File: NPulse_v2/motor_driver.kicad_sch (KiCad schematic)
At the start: 16 parts, among them J1 Screw_Terminal_01x02, Q1 PMOS, Q2 PMOS, Q3 NMOS, Q4 NMOS

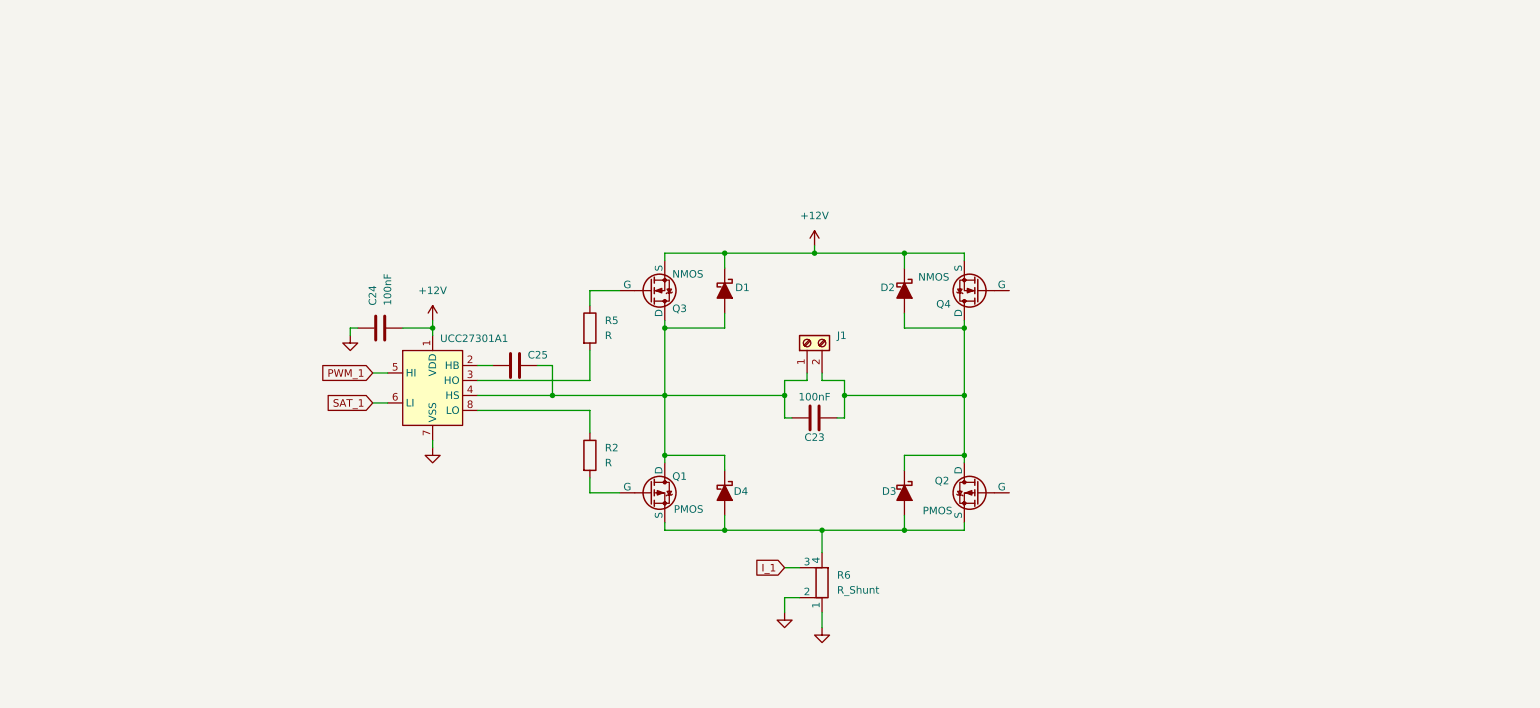
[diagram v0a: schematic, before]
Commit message: Add MCU, FSR, motor drivers, light sensing
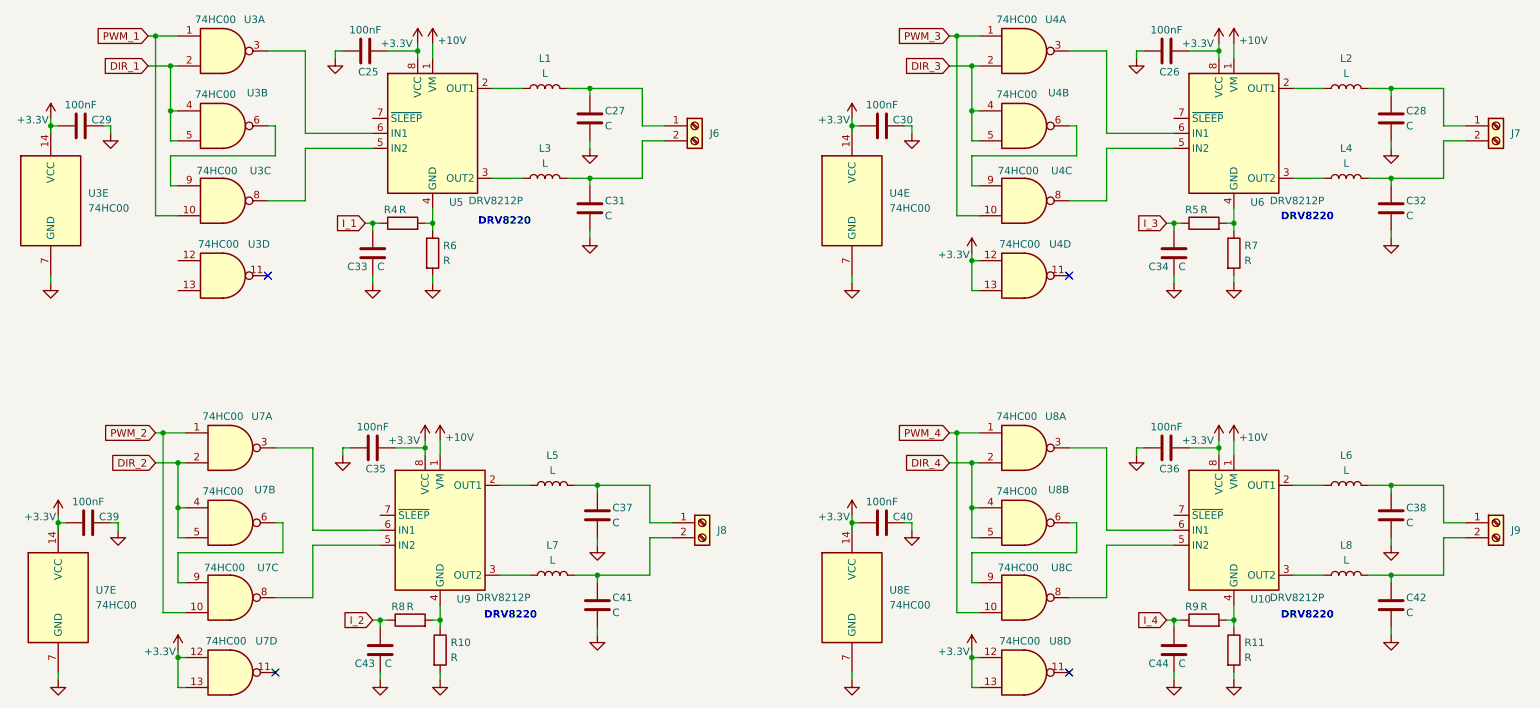
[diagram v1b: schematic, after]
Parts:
- removed C23, C24: 100nF, symbol Device:C
- removed D1, D2, D3, D4: D_Schottky_Filled, symbol Device:D_Schottky_Filled
- removed J1: Screw_Terminal_01x02, symbol Connector:Screw_Terminal_01x02
- removed Q1, Q2: PMOS, symbol Simulation_SPICE:PMOS
- removed Q3, Q4: NMOS, symbol Simulation_SPICE:NMOS
- removed R2: R, symbol Device:R
- removed R6: R_Shunt, symbol Device:R_Shunt
- removed UCC27301A1: U, symbol Driver_FET:UCC27301A
- added C26, C29, C30, C35, C36, C39, C40: 100nF, symbol Device:C
- added C27, C28, C31, C32, C33, C34, C37, C38, C41, C42, C43, C44: C, symbol Device:C
- added J6, J7, J8, J9: Screw_Terminal_01x02, symbol Connector:Screw_Terminal_01x02
- added L1, L2, L3, L4, L5, L6, L7, L8: L, symbol Device:L
- added R10, R11, R4, R6, R7, R8, R9: R, symbol Device:R
- added U10, U5, U6, U9: DRV8212P, Package_SON:WSON-8-1EP_2x2mm_P0.5mm_EP0.9x1.6mm_ThermalVias, symbol Driver_Motor:DRV8212P
- added U3, U4, U7, U8: 74HC00, symbol 74xx:74HC00
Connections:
- net GND: now also C25.1, C26.1, C27.2, C28.2, C29.2, C30.2, C31.2, C32.2, C33.2, C34.2, C35.1, C36.1, C37.2, C38.2, C39.2, C40.2, C41.2, C42.2, C43.2, C44.2, R10.2, R11.2, R6.2, R7.2, U3.7 (GND), U4.7 (GND), U7.7 (GND), U8.7 (GND)
- net I_1: now also C33.1, R4.1
- net PWM_1: now also U3.1, U3.10
- net +3.3V: now reaches C25.2
- net +3.3V: now also C26.2, C29.1, C30.1, C35.2, C36.2, C39.1, C40.1, U10.8 (VCC), U3.14 (VCC), U4.12, U4.13, U4.14 (VCC), U5.8 (VCC), U6.8 (VCC), U7.12, U7.13, U7.14 (VCC), U8.12, U8.13, U8.14 (VCC), U9.8 (VCC)
- net I_3: now reaches R5.1
- net I_3: now also C34.1
- net at R5.2: now also R7.1, U6.4 (GND), U6.9 (GND)
- new net: C28.1, J7.1 (Pin_1), L2.2
- new net: U3.8, U5.5 (IN2)
- new net: U3.6, U3.9
- new net: R10.1, R8.2, U9.4 (GND), U9.9 (GND)
- new net: L6.1, U10.2 (OUT1)
- new net: L8.1, U10.3 (OUT2)
- new net: R11.1, R9.2, U10.4 (GND), U10.9 (GND)
- new net: U10.5 (IN2), U8.8
- new net: U10.6 (IN1), U8.3
- new net: C42.1, J9.2 (Pin_2), L8.2
- new net: C37.1, J8.1 (Pin_1), L5.2
- new net: C41.1, J8.2 (Pin_2), L7.2
- new net: C38.1, J9.1 (Pin_1), L6.2
- new net: C32.1, J7.2 (Pin_2), L4.2
- new net: C31.1, J6.2 (Pin_2), L3.2
- new net: U8.6, U8.9
- new net: U4.8, U6.5 (IN2)
- new net: U4.6, U4.9
- new net: U7.3, U9.6 (IN1)
- new net: C27.1, J6.1 (Pin_1), L1.2
- new net: L3.1, U5.3 (OUT2)
- new net: U7.6, U7.9
- new net: L7.1, U9.3 (OUT2)
- new net: L4.1, U6.3 (OUT2)
- new net: U3.3, U5.6 (IN1)
- new net: L2.1, U6.2 (OUT1)
- new net: U4.3, U6.6 (IN1)
- new net: R4.2, R6.1, U5.4 (GND), U5.9 (GND)
- new net: L5.1, U9.2 (OUT1)
- new net: U7.8, U9.5 (IN2)
- new net: L1.1, U5.2 (OUT1)
- new net +10V: U10.1 (VM), U5.1 (VM), U6.1 (VM), U9.1 (VM)
- new net DIR_1: U3.2, U3.4, U3.5
- new net DIR_2: U7.2, U7.4, U7.5
- new net DIR_3: U4.2, U4.4, U4.5
- new net DIR_4: U8.2, U8.4, U8.5
- new net I_2: C43.1, R8.1
- new net I_4: C44.1, R9.1
- new net PWM_2: U7.1, U7.10
- new net PWM_3: U4.1, U4.10
- new net PWM_4: U8.1, U8.10
- no-connect marks 0 -> 4
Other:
- note added: "DRV8220"

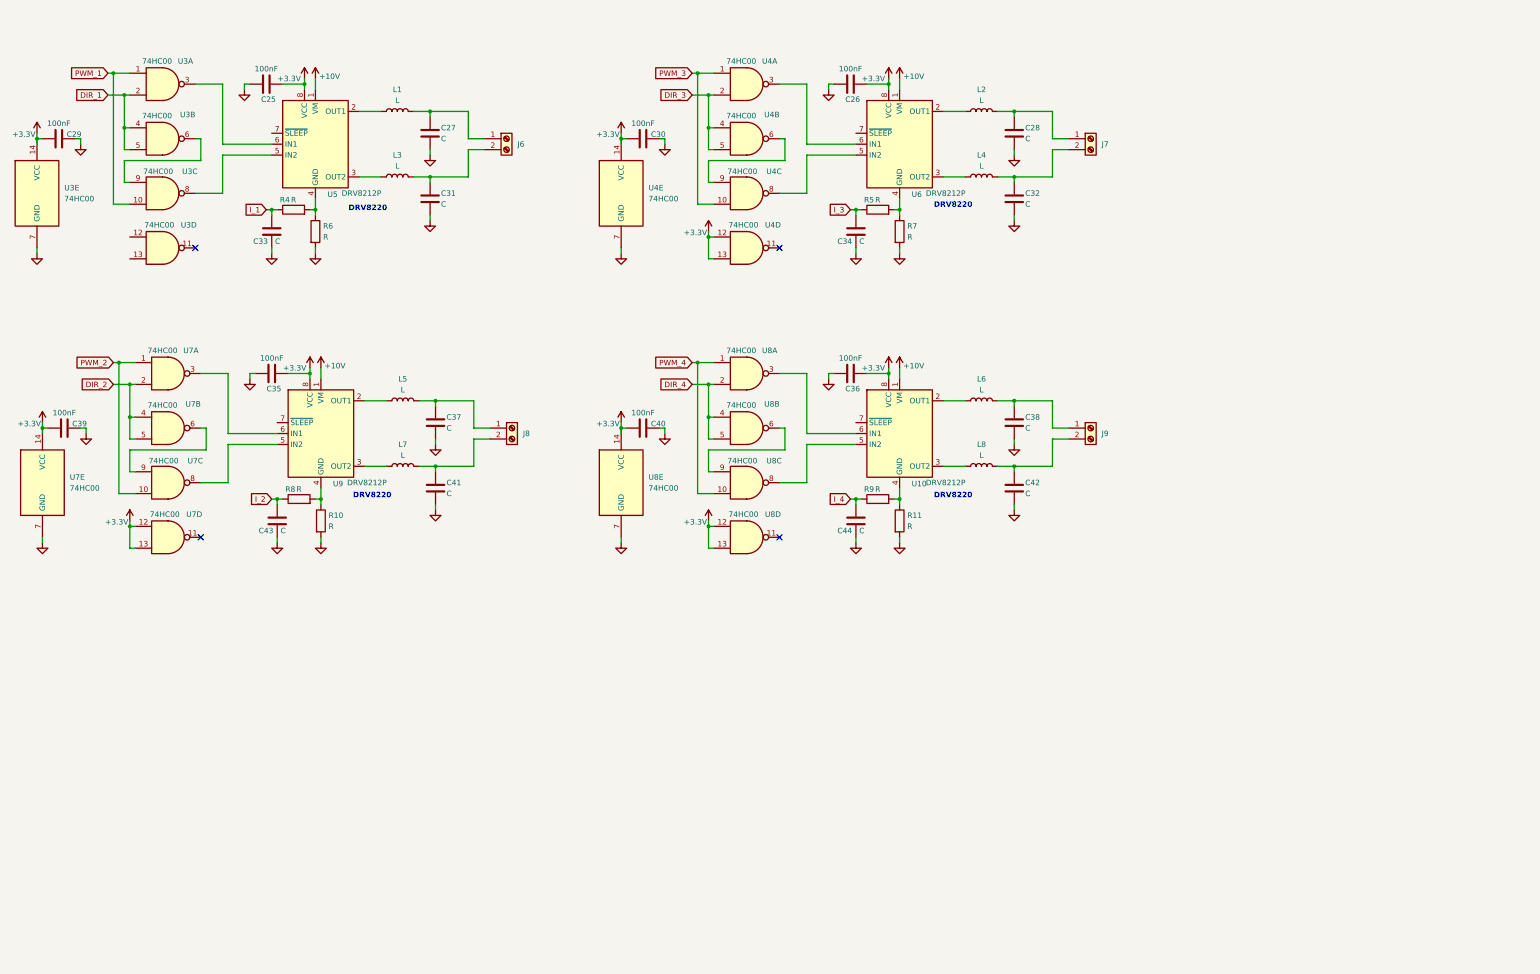
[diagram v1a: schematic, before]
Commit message: Version 3 - motor driver updated, FSR updated
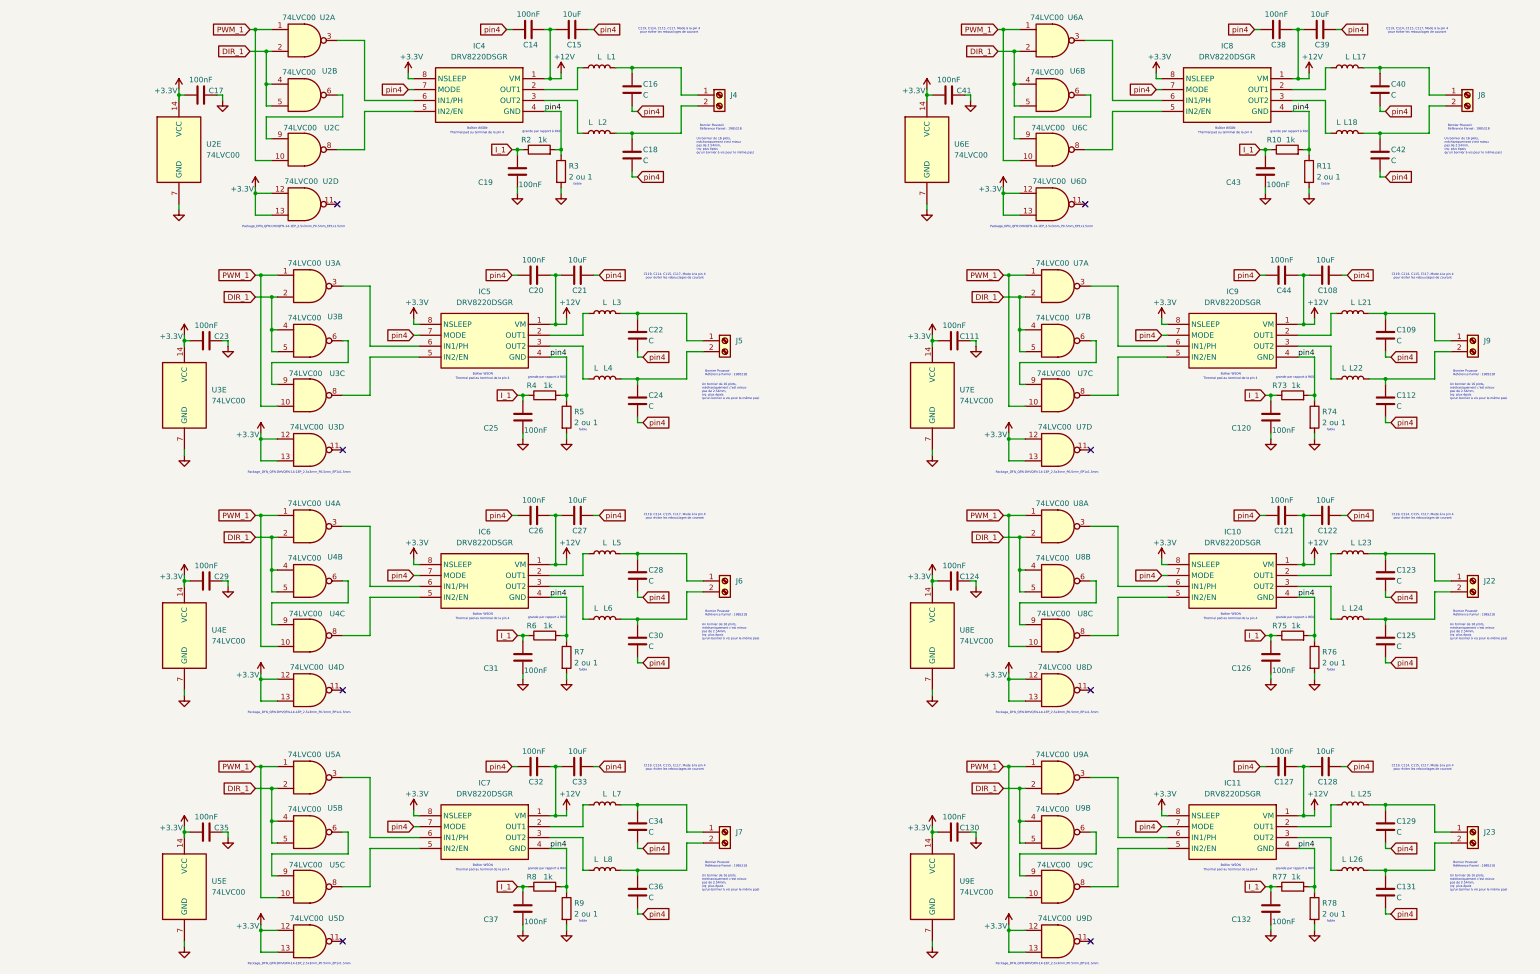
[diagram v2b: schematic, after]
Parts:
- removed U10, U5, U6, U9: DRV8212P, Package_SON:WSON-8-1EP_2x2mm_P0.5mm_EP0.9x1.6mm_ThermalVias, symbol Driver_Motor:DRV8212P
- added C108, C122, C128, C15, C21: 10uF, symbol Device:C
- added C109, C112, C123, C125, C129, C131, C16, C18, C22, C24: C, symbol Device:C
- added C111, C120, C121, C124, C126, C127, C130, C132, C14, C17, C19, C20, C23: 100nF, symbol Device:C
- added IC10, IC11, IC4, IC5, IC6, IC7, IC8, IC9: DRV8220DSGR, symbol DRV8220DSGR:DRV8220DSGR
- added J22, J23, J4, J5: Screw_Terminal_01x02, symbol Connector:Screw_Terminal_01x02
- added L17, L18, L21, L22, L23, L24, L25, L26: L, symbol Device:L
- added R2, R73, R75, R77: 1k, symbol Device:R
- added R3, R74, R76, R78: 2 ou 1, symbol Device:R
- added U2, U5, U6, U9: 74LVC00, symbol 74xx:74HC00
- C27, C33: value C -> 10uF
- C30, C36, C40: value 100nF -> C
- C31, C32, C37, C38, C41, C43, C44: value C -> 100nF
- C39: value 100nF -> 10uF
- R10, R4, R6, R8: value R -> 1k
- R11, R5, R7, R9: value R -> 2 ou 1
- U3, U4, U7, U8: value 74HC00 -> 74LVC00
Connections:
- net DIR_2 is gone; now on net DIR_1: U7.2, U7.4, U7.5
- net DIR_3 is gone; now on net DIR_1: U4.2, U4.4, U4.5
- net DIR_4 is gone; now on net DIR_1: U8.2, U8.4, U8.5
- net I_2 is gone; now on net I_1: C43.1, R8.1
- net I_4 is gone; now on net pin4: C44.1, R9.1
- net PWM_2 is gone; now on net PWM_1: U7.1, U7.10
- net PWM_3 is gone; now on net PWM_1: U4.1, U4.10
- net PWM_4 is gone; now on net PWM_1: U8.1, U8.10
- net +3.3V: now also C35.1, C41.1, U3.12, U3.13, C111.1, C124.1, C130.1, C17.1, C23.1, IC10.8 (NSLEEP), IC11.8 (NSLEEP), IC4.8 (NSLEEP), IC5.8 (NSLEEP), IC6.8 (NSLEEP), IC7.8 (NSLEEP), IC8.8 (NSLEEP), IC9.8 (NSLEEP), U2.12, U2.13, U2.14 (VCC), U5.12, U5.13, U5.14 (VCC), U6.12, U6.13, U6.14 (VCC), U9.12, U9.13, U9.14 (VCC); no longer C25.2, C26.2, C30.1, C35.2, C36.2, C39.1, C40.1
- net DIR_1: now also U2.2, U2.4, U2.5, U5.2, U5.4, U5.5, U6.2, U6.4, U6.5, U9.2, U9.4, U9.5
- net GND: now also C25.2, C35.2, R5.2, R9.2, C111.2, C120.2, C124.2, C126.2, C130.2, C132.2, C17.2, C19.2, C23.2, R3.2, R74.2, R76.2, R78.2, U2.7 (GND), U5.7 (GND), U6.7 (GND), U9.7 (GND); no longer C25.1, C26.1, C27.2, C28.2, C30.2, C32.2, C33.2, C34.2, C35.1, C36.1, C38.2, C39.2, C40.2, C42.2, C44.2, R10.2, R6.2
- net I_1: now also C25.1, C31.1, C37.1, R10.1, R6.1, C120.1, C126.1, C132.1, C19.1, R2.1, R73.1, R75.1, R77.1; no longer C33.1
- net PWM_1: now also U2.1, U2.10, U5.1, U5.10, U6.1, U6.10, U9.1, U9.10
- net at U3.8: now also IC5.5 (IN2/EN)
- net pin4: now reaches R8.2
- net pin4: now also C26.1, C27.2, C28.2, C30.2, C32.1, C33.2, C34.2, C36.2, C38.1, C39.2, C40.2, C42.2, R10.2, R11.1, R4.2, R5.1, R6.2, R7.1, C108.2, C109.2, C112.2, C121.1, C122.2, C123.2, C125.2, C127.1, C128.2, C129.2, C131.2, C14.1, C15.2, C16.2, C18.2, C20.1, C21.2, C22.2, C24.2, IC10.4 (GND), IC10.7 (MODE), IC11.4 (GND), IC11.7 (MODE), IC4.4 (GND), IC4.7 (MODE), IC5.4 (GND), IC5.7 (MODE), IC6.4 (GND), IC6.7 (MODE), IC7.4 (GND), IC7.7 (MODE), IC8.4 (GND), IC8.7 (MODE), IC9.4 (GND), IC9.7 (MODE), R2.2, R3.1, R73.2, R74.1, R75.2, R76.1, R77.2, R78.1; no longer R10.1
- net at L6.1: now also IC6.3 (OUT2)
- net at L8.1: now also IC7.3 (OUT2)
- net at U8.8: now also IC10.5 (IN2/EN)
- net at U8.3: now also IC10.6 (IN1/PH)
- net at U4.8: now also IC6.5 (IN2/EN)
- net at U7.3: now also IC9.6 (IN1/PH)
- net at L3.1: now also IC5.2 (OUT1)
- net at L7.1: now also IC7.2 (OUT1)
- net at L4.1: now also IC5.3 (OUT2)
- net at U3.3: now also IC5.6 (IN1/PH)
- net at L2.1: now also IC4.3 (OUT2)
- net at U4.3: now also IC6.6 (IN1/PH)
- net at L5.1: now also IC6.2 (OUT1)
- net at U7.8: now also IC9.5 (IN2/EN)
- net at L1.1: now also IC4.2 (OUT1)
- net I_3: no longer names the net of C34.1
- net I_3: now also J7.1 (Pin_1), L7.2; no longer R5.1
- new net: C16.1, J4.1 (Pin_1), L1.2
- new net: IC11.6 (IN1/PH), U9.3
- new net: C30.1, J6.2 (Pin_2), L6.2
- new net: IC4.5 (IN2/EN), U2.8
- new net: IC4.6 (IN1/PH), U2.3
- new net: IC7.5 (IN2/EN), U5.8
- new net: U5.6, U5.9
- new net: C131.1, J23.2 (Pin_2), L26.2
- new net: C129.1, J23.1 (Pin_1), L25.2
- new net: U6.6, U6.9
- new net: IC11.2 (OUT1), L25.1
- new net: C40.1, J8.1 (Pin_1), L17.2
- new net: IC9.3 (OUT2), L22.1
- new net: C112.1, J9.2 (Pin_2), L22.2
- new net: IC8.3 (OUT2), L18.1
- new net: C42.1, J8.2 (Pin_2), L18.2
- new net: C36.1, J7.2 (Pin_2), L8.2
- new net: IC11.3 (OUT2), L26.1
- new net: IC11.5 (IN2/EN), U9.8
- new net: C125.1, J22.2 (Pin_2), L24.2
- new net: C22.1, J5.1 (Pin_1), L3.2
- new net: U9.6, U9.9
- new net: C18.1, J4.2 (Pin_2), L2.2
- new net: IC7.6 (IN1/PH), U5.3
- new net: IC9.2 (OUT1), L21.1
- new net: C109.1, J9.1 (Pin_1), L21.2
- new net: IC8.2 (OUT1), L17.1
- new net: IC8.5 (IN2/EN), U6.8
- new net: IC8.6 (IN1/PH), U6.3
- new net: C24.1, J5.2 (Pin_2), L4.2
- new net: U2.6, U2.9
- new net: C123.1, J22.1 (Pin_1), L23.2
- new net: IC10.3 (OUT2), L24.1
- new net: IC10.2 (OUT1), L23.1
- new net: C28.1, J6.1 (Pin_1), L5.2
- new net +12V: C108.1, C121.2, C122.1, C127.2, C128.1, C14.2, C15.1, C20.2, C21.1, C26.2, C27.1, C32.2, C33.1, C38.2, C39.1, C44.2, IC10.1 (VM), IC11.1 (VM), IC4.1 (VM), IC5.1 (VM), IC6.1 (VM), IC7.1 (VM), IC8.1 (VM), IC9.1 (VM)
- no-connect marks 4 -> 8
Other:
- note added: "Bornier Poussoir Référence Farnel : 1985218"
- note added: "Boîtier WSON"
- note added: "C119, C114, C115, C117, Mode à la pin 4 pour éviter les rebouclages de courant"
- note added: "Package_DFN_QFN:DHVQFN-14-1EP_2.5x3mm_P0.5mm_EP1x1.5mm"
- note added: "Thermal pad au terminal de la pin 4"
- note added: "Un bornier de 16 plots, méchaniquement c'est mieux pas de 2.54mm, (rq: plus épais qu'un bornier à vis pour le même pas)"
- note added: "faible"
- note added: "grande par rapport à R60"
- note removed: "DRV8220"
